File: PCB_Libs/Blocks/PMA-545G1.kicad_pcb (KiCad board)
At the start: 2 copper layers, 14 parts, among them U1 PMA-545G1_Amp

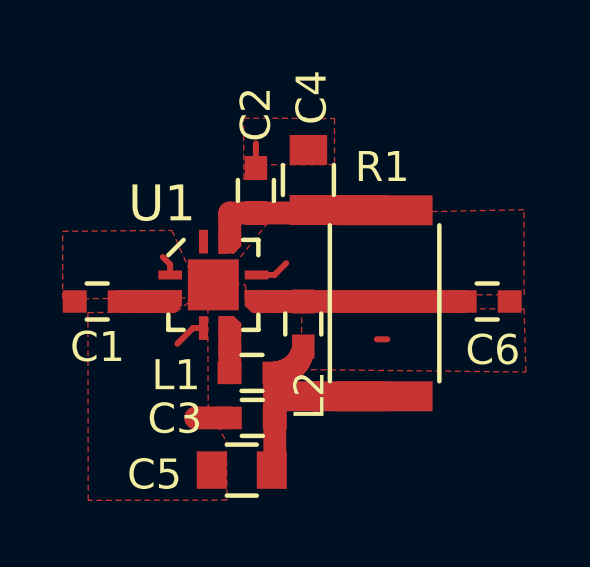
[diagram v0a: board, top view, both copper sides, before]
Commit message: [Added] Minicircuits footprint test project; [Modified] amplifier block to include stitching vias
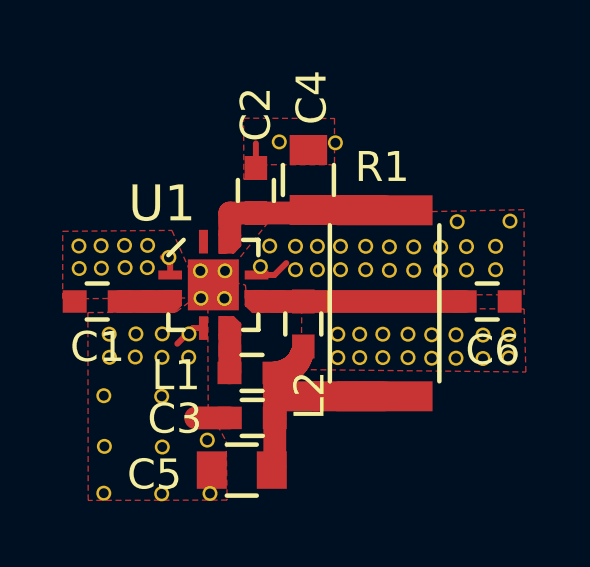
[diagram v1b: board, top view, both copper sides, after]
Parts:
- added ?: , DigitalLogic:Via, F.Cu at (143.3, 87.7)
- added ?: , DigitalLogic:Via, F.Cu at (137.5, 96.2)
- added ?: , DigitalLogic:Via, F.Cu at (146.5, 94.9)
- added ?: , DigitalLogic:Via, F.Cu at (145.7, 94.9)
- added ?: , DigitalLogic:Via, F.Cu at (146.5, 94.1)
- added ?: , DigitalLogic:Via, F.Cu at (145.7, 94.1)
- added ?: , DigitalLogic:Via, F.Cu at (148.2, 94.9)
- added ?: , DigitalLogic:Via, F.Cu at (147.3, 94.9)
- added ?: , DigitalLogic:Via, F.Cu at (148.2, 94.1)
- added ?: , DigitalLogic:Via, F.Cu at (147.3, 94.1)
- added ?: , DigitalLogic:Via, F.Cu at (149.0, 94.9)
- added ?: , DigitalLogic:Via, F.Cu at (141.4, 87.7)
- added ?: , DigitalLogic:Via, F.Cu at (149.0, 94.1)
- added ?: , DigitalLogic:Via, F.Cu at (144.8, 94.9)
- added ?: , DigitalLogic:Via, F.Cu at (144.8, 94.1)
- added ?: , DigitalLogic:Via, F.Cu at (143.3, 94.9)
- added ?: , DigitalLogic:Via, F.Cu at (144.1, 94.9)
- added ?: , DigitalLogic:Via, F.Cu at (144.1, 94.1)
- added ?: , DigitalLogic:Via, F.Cu at (143.3, 94.1)
- added ?: , DigitalLogic:Via, F.Cu at (149.1, 90.3)
- added ?: , DigitalLogic:Via, F.Cu at (147.3, 90.3)
- added ?: , DigitalLogic:Via, F.Cu at (148.6, 91.2)
- added ?: , DigitalLogic:Via, F.Cu at (139.1, 99.4)
- added ?: , DigitalLogic:Via, F.Cu at (148.6, 92.0)
- added ?: , DigitalLogic:Via, F.Cu at (147.6, 91.2)
- added ?: , DigitalLogic:Via, F.Cu at (147.6, 92.0)
- added ?: , DigitalLogic:Via, F.Cu at (146.8, 91.2)
- added ?: , DigitalLogic:Via, F.Cu at (146.8, 92.0)
- added ?: , DigitalLogic:Via, F.Cu at (145.9, 91.2)
- added ?: , DigitalLogic:Via, F.Cu at (145.9, 92.0)
- added ?: , DigitalLogic:Via, F.Cu at (145.1, 91.2)
- added ?: , DigitalLogic:Via, F.Cu at (145.1, 92.0)
- added ?: , DigitalLogic:Via, F.Cu at (144.3, 91.2)
- added ?: , DigitalLogic:Via, F.Cu at (139.0, 97.6)
- added ?: , DigitalLogic:Via, F.Cu at (144.3, 92.0)
- added ?: , DigitalLogic:Via, F.Cu at (143.4, 91.2)
- added ?: , DigitalLogic:Via, F.Cu at (143.4, 92.0)
- added ?: , DigitalLogic:Via, F.Cu at (142.7, 91.2)
- added ?: , DigitalLogic:Via, F.Cu at (142.7, 92.0)
- added ?: , DigitalLogic:Via, F.Cu at (138.4, 94.1)
- added ?: , DigitalLogic:Via, F.Cu at (138.4, 94.9)
- added ?: , DigitalLogic:Via, F.Cu at (137.7, 91.5)
- added ?: , DigitalLogic:Via, F.Cu at (134.7, 91.2)
- added ?: , DigitalLogic:Via, F.Cu at (134.7, 91.9)
- added ?: , DigitalLogic:Via, F.Cu at (135.5, 96.2)
- added ?: , DigitalLogic:Via, F.Cu at (135.7, 94.9)
- added ?: , DigitalLogic:Via, F.Cu at (136.6, 94.9)
- added ?: , DigitalLogic:Via, F.Cu at (137.5, 94.9)
- added ?: , DigitalLogic:Via, F.Cu at (137.5, 94.1)
- added ?: , DigitalLogic:Via, F.Cu at (136.6, 94.1)
- added ?: , DigitalLogic:Via, F.Cu at (135.7, 94.1)
- added ?: , DigitalLogic:Via, F.Cu at (137.0, 91.1)
- added ?: , DigitalLogic:Via, F.Cu at (136.2, 91.1)
- added ?: , DigitalLogic:Via, F.Cu at (135.4, 91.2)
- added ?: , DigitalLogic:Via, F.Cu at (135.5, 91.9)
- added ?: , DigitalLogic:Via, F.Cu at (135.6, 97.8)
- added ?: , DigitalLogic:Via, F.Cu at (136.2, 91.9)
- added ?: , DigitalLogic:Via, F.Cu at (137.0, 91.9)
- added ?: , DigitalLogic:Via, F.Cu at (141.9, 91.2)
- added ?: , DigitalLogic:Via, F.Cu at (141.9, 92.0)
- added ?: , DigitalLogic:Via, F.Cu at (141.1, 91.2)
- added ?: , DigitalLogic:Via, F.Cu at (140.8, 91.8)
- added ?: , DigitalLogic:Via, F.Cu at (138.8, 92.9)
- added ?: , DigitalLogic:Via, F.Cu at (139.6, 92.9)
- added ?: , DigitalLogic:Via, F.Cu at (139.6, 92.0)
- added ?: , DigitalLogic:Via, F.Cu at (138.8, 92.0)
- added ?: , DigitalLogic:Via, F.Cu at (135.5, 99.4)
- added ?: , DigitalLogic:Via, F.Cu at (137.5, 99.4)
- added ?: , DigitalLogic:Via, F.Cu at (137.5, 97.9)
